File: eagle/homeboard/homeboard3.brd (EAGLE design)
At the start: 100 x 80 mm, 81 parts, among them IC1 XCF02S, IC2 25LC080SN, Q5 BC848SMD, Q6 BC848SMD, Q7 BC848SMD, Q8 BC848SMD, T1 BSS138, T2 BC848, T3 BSS138, U1 XC3S400TQ144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

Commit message: maybe gonna go into work now
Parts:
- moved R13 40.8 mm to (5.00, 21.0), turned to 0 degrees
- moved R14 40.2 mm to (5.00, 23.5), turned to 0 degrees
- moved Q5 40.0 mm to (5.00, 27.0), turned to 0 degrees
- moved R8 35.7 mm to (8.00, 27.0), turned to 270 degrees
- moved R1 33.3 mm to (10.2, 68.5)
- moved R3 33.3 mm to (24.7, 69.0)
- moved R2 33.3 mm to (27.6, 69.0)
- moved REG1.2 33.3 mm to (17.0, 57.0)
- moved REG2.5 33.3 mm to (21.5, 51.8)
- moved U$1 33.3 mm to (39.8, 54.7)
- moved U1 33.3 mm to (19.2, 54.3)
- moved IC1 33.3 mm to (41.1, 51.5)
- moved R15 31.9 mm to (11.5, 20.8), turned to 0 degrees
- moved X2 31.7 mm to (21.0, 8.00), turned to 180 degrees
- moved R20 31.2 mm to (11.5, 23.0), turned to 0 degrees
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
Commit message: rough positioning
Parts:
- moved X1 133.3 mm to (96.0, -8.00), turned to 180 degrees
- moved IC1 21.6 mm to (59.1, 39.5)
- moved R1 21.6 mm to (28.2, 56.5)
- moved R2 21.6 mm to (45.6, 57.0)
- moved R3 21.6 mm to (42.7, 57.0)
- moved REG1.2 21.6 mm to (35.0, 45.0)
- moved REG2.5 21.6 mm to (39.5, 39.8)
- moved U$1 21.6 mm to (57.8, 42.7)
- moved U1 21.6 mm to (37.2, 42.3)
- moved Q6 19.1 mm to (28.8, 20.5)
- moved Q8 18.8 mm to (36.5, 20.5)
- moved Q7 17.4 mm to (44.0, 20.5)
- moved R10 17.3 mm to (29.8, 20.8), flipped to the top
- moved R23 17.3 mm to (49.2, 22.0)
- moved R34 17.1 mm to (53.2, 22.0), turned to 270 degrees
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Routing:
- net SCART_BLANKING: track 37.6 -> 0.00 mm, vias 2 -> 0
- net SCART_MODE: track 22.5 -> 0.00 mm, vias 2 -> 0
- net SCART_BLUE: track 25.1 -> 4.67 mm
- net SCART_RED: track 23.4 -> 4.50 mm
- net SCART_GREEN: track 23.1 -> 4.50 mm
- net SCART_COMP: track 20.7 -> 2.25 mm
- net GND: track 234.3 -> 217.0 mm
- net SCART_LEFT: track 18.6 -> 9.72 mm
- net SCART_RIGHT: track 18.5 -> 9.64 mm
- net N$55: track 6.59 -> 0.00 mm
- net N$51: track 4.78 -> 0.00 mm
- net N$65: track 4.89 -> 0.49 mm
- net N$57: track 4.20 -> 0.00 mm
- net N$53: track 4.15 -> 0.00 mm
- net N$59: track 4.90 -> 2.25 mm
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
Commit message: moving things around
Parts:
- moved U$2 55.1 mm to (32.6, 26.9)
- moved IC1 7.62 mm to (56.1, 46.5)
- moved R1 7.62 mm to (25.2, 63.5)
- moved R2 7.62 mm to (42.6, 64.0)
- moved R3 7.62 mm to (39.7, 64.0)
- moved REG1.2 7.62 mm to (32.0, 52.0)
- moved REG2.5 7.62 mm to (36.5, 46.8)
- moved U$1 7.62 mm to (54.8, 49.7)
- moved U1 7.62 mm to (34.2, 49.3)
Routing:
- net VCC: track 179.4 -> 202.5 mm
- net SCART_COMP: track 2.25 -> 12.6 mm
- net SCART_RED: track 4.50 -> 14.7 mm
- net SCART_GREEN: track 4.50 -> 14.6 mm
- net SCART_BLUE: track 4.67 -> 14.5 mm
- net N$59: track 2.25 -> 7.00 mm
- net N$54: track 4.50 -> 7.50 mm
- net N$58: track 4.50 -> 7.50 mm
- net N$56: track 4.50 -> 7.50 mm

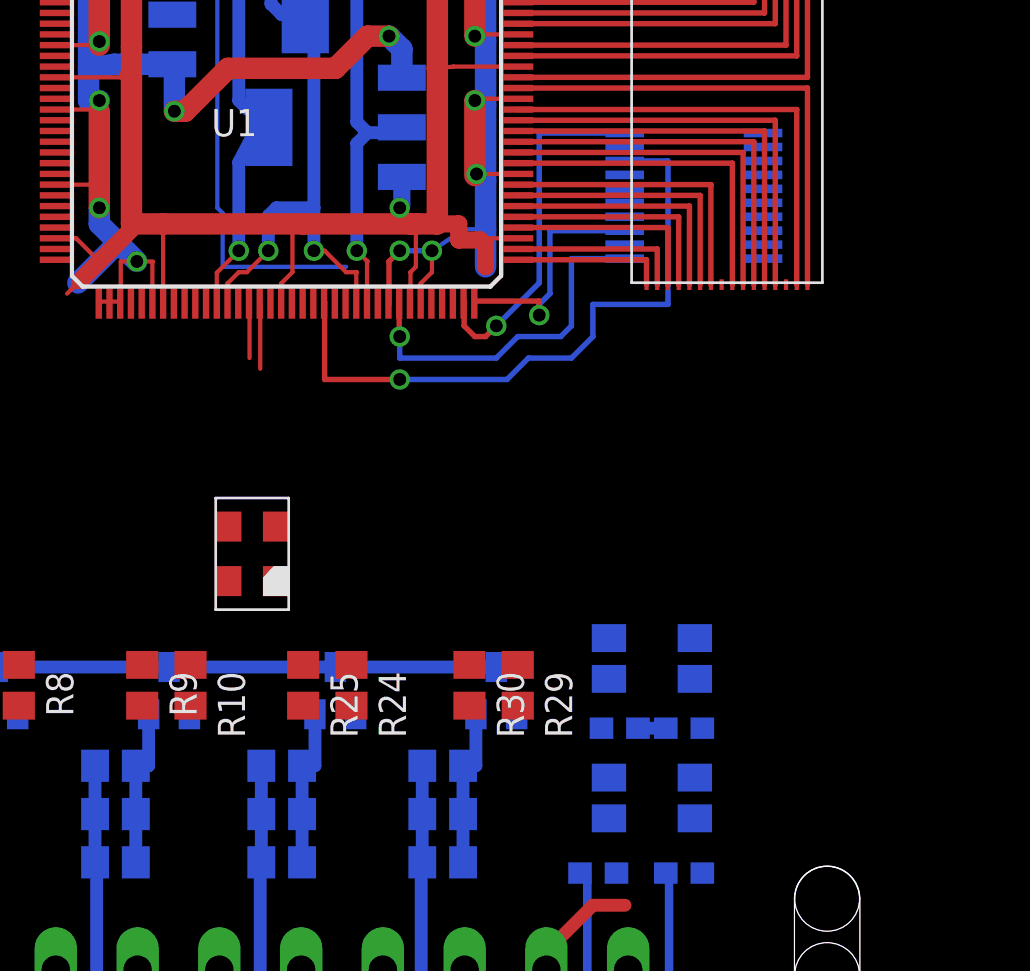
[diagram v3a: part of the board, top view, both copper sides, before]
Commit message: moved prom out
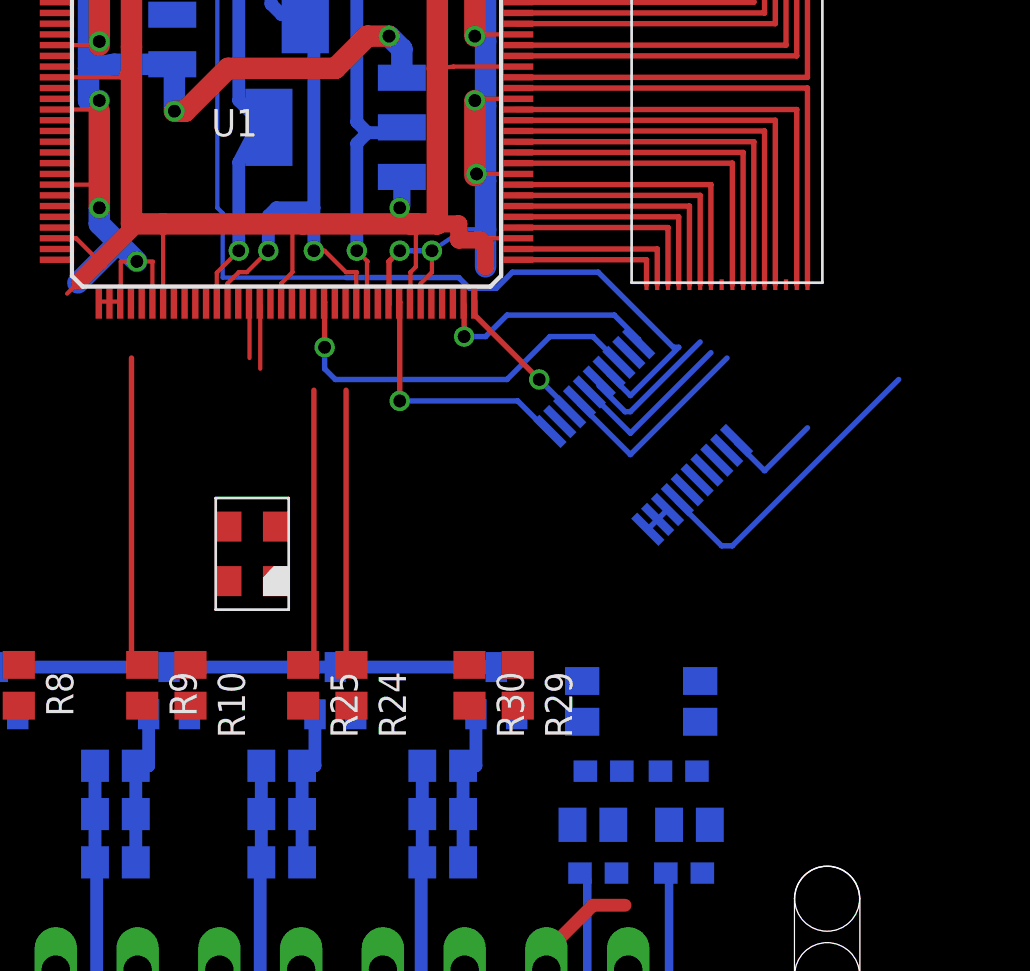
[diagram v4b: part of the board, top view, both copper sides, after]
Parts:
- moved IC1 14.2 mm to (55.0, 32.4), turned to 315 degrees
- moved R23 2.36 mm to (48.0, 20.0)
- moved C1 2.14 mm to (49.0, 16.8)
- moved C5 2.02 mm to (52.5, 16.8)
- moved R34 2.02 mm to (53.5, 20.0)
- moved R48 1.46 mm to (48.5, 14.2), turned to 180 degrees
- moved R49 1.27 mm to (53.0, 14.2), turned to 180 degrees
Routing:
- net N$40: track 29.5 -> 52.1 mm
- net R1: track 0.00 -> 14.8 mm
- net N$36: track 0.00 -> 14.5 mm
- net G0: track 0.00 -> 13.3 mm
- net G1: track 0.00 -> 13.1 mm
- net PROM_INITB: track 30.7 -> 18.4 mm
- net TDI: track 0.00 -> 9.81 mm
- net TMS: track 0.00 -> 8.02 mm
- net TCK: track 0.00 -> 6.72 mm
- net N$38: track 16.9 -> 10.7 mm
- net PROM_DO: track 16.9 -> 12.2 mm
- net N$35: track 11.3 -> 7.02 mm
- net GND: track 217.0 -> 219.3 mm
- net VCC: track 202.5 -> 203.8 mm

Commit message: mah
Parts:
- removed JP1: (no value), jumper:JP1
- added WR_PROT: (no value), jumper:JP1
- moved IC2 47.8 mm to (50.0, 28.0), turned to 315 degrees
- moved R47 27.3 mm to (76.5, 27.5)
- moved RESET_SW 14.8 mm to (69.5, 18.0), turned to 270 degrees
- moved IC1 4.03 mm to (59.0, 32.9)
- moved C5 2.00 mm to (54.5, 16.8)
- moved R23 1.75 mm to (49.8, 20.0), flipped to the top, turned to 180 degrees
- moved C3 1.50 mm to (47.2, 12.0), turned to 180 degrees
- moved R49 1.50 mm to (54.5, 14.2), turned to 0 degrees
- moved R34 1.00 mm to (54.5, 20.0), flipped to the top, turned to 0 degrees
- moved R48 1.00 mm to (47.5, 14.2), turned to 0 degrees
- moved C1 0.50 mm to (49.5, 16.8)
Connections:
- net GND: now also WR_PROT.1; no longer JP1.1
- net N$49: now also WR_PROT.2; no longer JP1.2
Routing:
- net N$36: track 14.5 -> 49.6 mm
- net TCK: track 6.72 -> 30.4 mm
- net MISO: track 0.00 -> 19.3 mm
- net N$49: track 0.00 -> 15.7 mm
- net CSYNC: track 3.91 -> 18.3 mm
- net R0: track 0.00 -> 14.1 mm
- net TDI: track 9.81 -> 23.8 mm
- net TMS: track 8.02 -> 21.2 mm
- net G1: track 13.1 -> 0.00 mm
- net MOSI: track 0.00 -> 10.8 mm, vias 0 -> 1
- net SCLK: track 0.00 -> 10.2 mm, vias 0 -> 1
- net VCC: track 203.8 -> 210.7 mm
- net GND: track 219.3 -> 225.1 mm
- net PROM_INITB: track 18.4 -> 22.1 mm
- net PROM_DO: track 12.2 -> 15.7 mm
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
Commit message: mah
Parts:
- moved IC1 11.6 mm to (57.8, 44.4), turned to 270 degrees
- moved IC2 8.61 mm to (54.9, 35.1), turned to 270 degrees
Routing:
- net GND: track 225.1 -> 271.5 mm, vias 17 -> 20
- net N$40: track 55.4 -> 22.1 mm, vias 1 -> 0
- net N$36: track 49.6 -> 24.3 mm
- net N$49: track 15.7 -> 0.58 mm
- net VCC: track 210.7 -> 221.5 mm, vias 4 -> 5
- net N$38: track 14.0 -> 4.77 mm
- net PROM_INITB: track 22.1 -> 13.6 mm
- net TCK: track 30.4 -> 22.7 mm
- net MOSI: track 10.8 -> 3.49 mm
- net SCLK: track 10.2 -> 3.52 mm
- net N$51: track 0.00 -> 6.52 mm, vias 0 -> 1
- net N$65: track 0.00 -> 6.29 mm, vias 0 -> 1
- net PROM_DO: track 15.7 -> 10.2 mm
- net FPGA_AUDIO_RIGHT: track 0.00 -> 4.93 mm
- net FPGA_AUDIO_LEFT: track 0.00 -> 4.29 mm
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
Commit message: mah
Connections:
- net MISO: now also U1.P63
- net MOSI: now also U1.P69
- net SCLK: now also U1.P70
- net SPI_SEL0: now also U1.P68
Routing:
- net VCCAUX: track 23.6 -> 0.00 mm, vias 2 -> 0
- net MOSI: track 3.49 -> 15.3 mm
- net N$38: track 4.77 -> 16.2 mm
- net SCLK: track 3.52 -> 13.8 mm
- net PROM_INITB: track 13.6 -> 23.2 mm
